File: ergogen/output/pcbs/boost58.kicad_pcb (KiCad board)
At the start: 2 copper layers, 153.6 x 133.5 mm, 110 parts, among them SW1 %R, SW10 %R, SW11 %R, SW12 %R, SW13 %R, SW14 %R, SW15 %R, SW16 %R, SW17 %R, SW18 %R, SW19 %R, SW2 %R, SW20 %R, SW21 %R, SW22 %R, SW23 %R, SW24 %R, SW25 %R, SW26 %R, SW27 %R, SW28 %R, SW29 %R, SW3 %R, SW4 %R, SW5 %R, SW6 %R, SW7 %R, SW8 %R, SW9 %R

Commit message: re-generated PCB
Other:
- board size 153.6 x 133.5 mm -> 147.8 x 127.7 mm

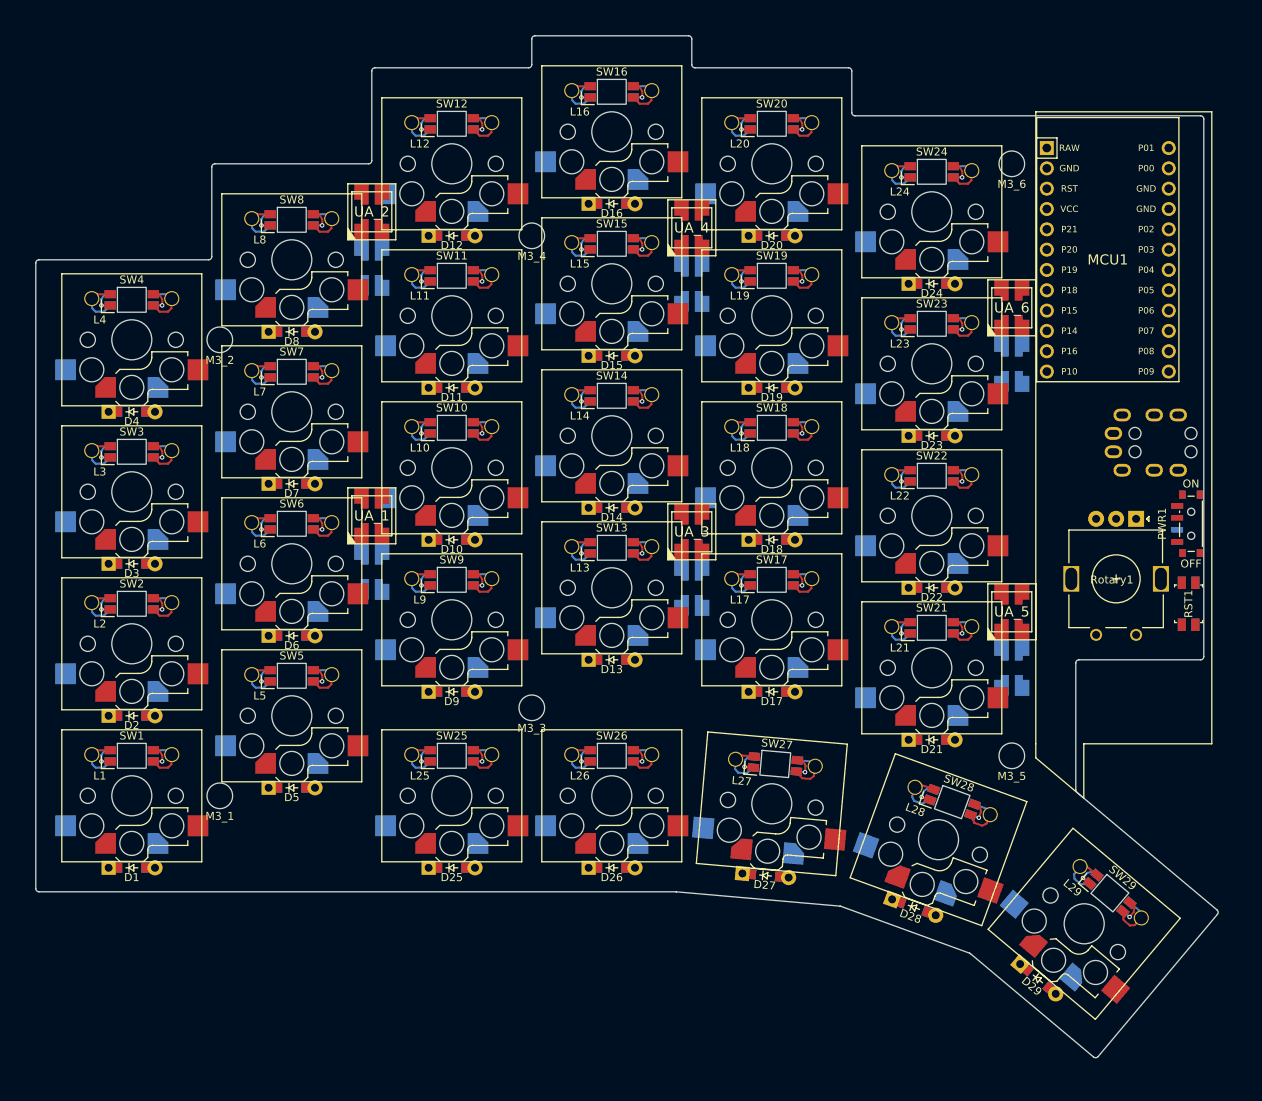
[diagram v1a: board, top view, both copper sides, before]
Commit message: re-generated PCB, and re-ran FreeRouting
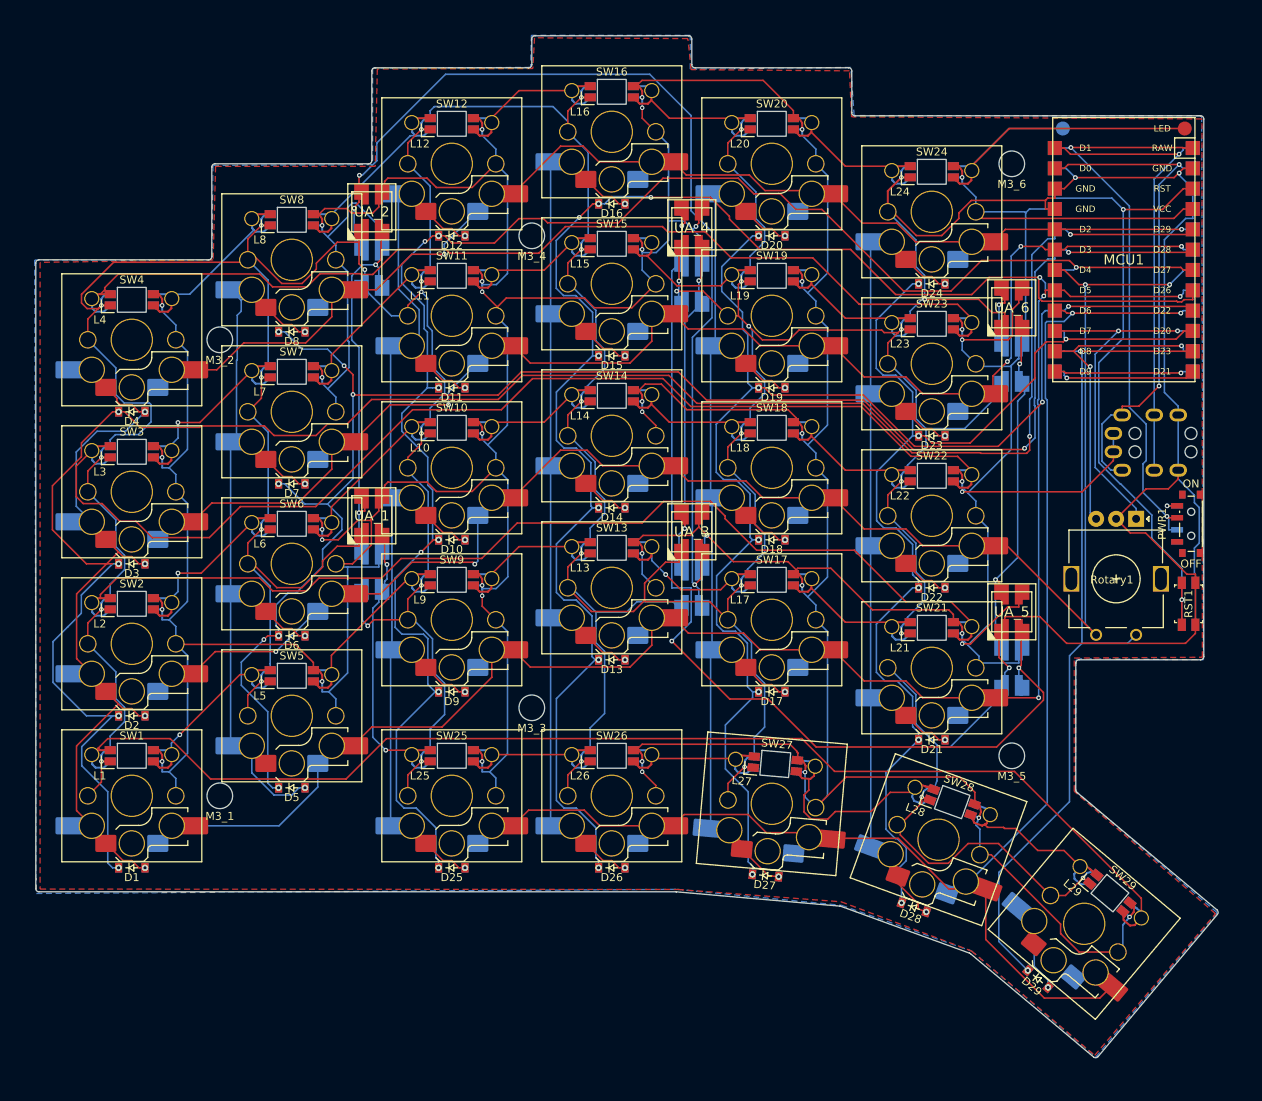
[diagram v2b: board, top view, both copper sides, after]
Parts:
- D1, D10, D11, D12, D13, D14, D15, D16, D17, D18, D19, D2, D20, D21, D22, D23, D24, D25, D26, D27, D28, D29, D3, D4, D5, D6, D7, D8, D9, L1, L10, L11, L12, L13, L14, L15, L16, L17, L18, L19, L2, L20, L21, L22, L23, L24, L25, L26, L27, L28, L29, L3, L4, L5, L6, L7, L8, L9, SW1, SW10, SW11, SW12, SW13, SW14, SW15, SW16, SW17, SW18, SW19, SW2, SW20, SW21, SW22, SW23, SW24, SW25, SW26, SW27, SW28, SW29, SW3, SW4, SW5, SW6, SW7, SW8, SW9: value %R -> ${REFERENCE}
- MCU1: footprint ProMicro -> SparkFunProMicroQwiic
- moved MCU1 2.00 mm to (164.0, 53.0)
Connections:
- net DP14 renamed DD20
- net DP15 renamed DD22
- net DP16 renamed DD23
- net DP18 renamed DD26
- net DP19 renamed DD27
- net DP20 renamed DD28
- net DP21 renamed DD29
- net P1001 renamed LED01
- net P10u01 renamed LEDu01
- net P10u02 renamed LEDu02
- net P10u03 renamed LEDu03
- net P10u04 renamed LEDu04
- net P10u05 renamed LEDu05
- net P10u06 renamed LEDu06
- D1 pad 1: P21 -> D29
- D10 pad 1: P19 -> D27
- D11 pad 1: P19 -> D27
- D12 pad 1: P19 -> D27
- D13 pad 1: P18 -> D26
- D14 pad 1: P18 -> D26
- D15 pad 1: P18 -> D26
- D16 pad 1: P18 -> D26
- D17 pad 1: P15 -> D22
- D18 pad 1: P15 -> D22
- D19 pad 1: P15 -> D22
- D2 pad 1: P21 -> D29
- D20 pad 1: P15 -> D22
- D21 pad 1: P14 -> D20
- D22 pad 1: P14 -> D20
- D23 pad 1: P14 -> D20
- D24 pad 1: P14 -> D20
- D25 pad 1: P19 -> D27
- D26 pad 1: P18 -> D26
- D27 pad 1: P15 -> D22
- D28 pad 1: P14 -> D20
- D29 pad 1: P16 -> D23
- D3 pad 1: P21 -> D29
- D4 pad 1: P21 -> D29
- D5 pad 1: P20 -> D28
- D6 pad 1: P20 -> D28
- D7 pad 1: P20 -> D28
- D8 pad 1: P20 -> D28
- D9 pad 1: P19 -> D27
- L1 pad 2: P1011 -> LED11
- L1 pad 4: P1010 -> LED10
- L10 pad 2: P1023 -> LED23
- L10 pad 4: P1022 -> LED22
- L11 pad 2: P1033 -> LED33
- L11 pad 4: P1032 -> LED32
- L12 pad 2: P1043 -> LED43
- L12 pad 4: P1042 -> LED42
- L13 pad 2: P1014 -> LED14
- L13 pad 4: P1013 -> LED13
- L14 pad 2: P1024 -> LED24
- L14 pad 4: P1023 -> LED23
- L15 pad 2: P1034 -> LED34
- L15 pad 4: P1033 -> LED33
- L16 pad 2: P1044 -> LED44
- L16 pad 4: P1043 -> LED43
- L17 pad 2: P1015 -> LED15
- L17 pad 4: P1014 -> LED14
- L18 pad 2: P1025 -> LED25
- L18 pad 4: P1024 -> LED24
- L19 pad 2: P1035 -> LED35
- L19 pad 4: P1034 -> LED34
- L2 pad 2: P1021 -> LED21
- L2 pad 4: P1020 -> LED20
- L20 pad 2: P1045 -> LED45
- L20 pad 4: P1044 -> LED44
- L21 pad 2: P1020 -> LED20
- L21 pad 4: P1015 -> LED15
- L22 pad 2: P1030 -> LED30
- L22 pad 4: P1025 -> LED25
- L23 pad 2: P1040 -> LED40
- L23 pad 4: P1035 -> LED35
- L24 pad 2: P10 -> LED
- L24 pad 4: P1045 -> LED45
- L25 pad 2: P1002 -> LED02
- L26 pad 2: P1003 -> LED03
- L26 pad 4: P1002 -> LED02
- L27 pad 2: P1004 -> LED04
- L27 pad 4: P1003 -> LED03
- L28 pad 2: P1005 -> LED05
- L28 pad 4: P1004 -> LED04
- L29 pad 2: P1010 -> LED10
- L29 pad 4: P1005 -> LED05
- L3 pad 2: P1031 -> LED31
- L3 pad 4: P1030 -> LED30
- L4 pad 2: P1041 -> LED41
- L4 pad 4: P1040 -> LED40
- L5 pad 2: P1012 -> LED12
- L5 pad 4: P1011 -> LED11
- L6 pad 2: P1022 -> LED22
- L6 pad 4: P1021 -> LED21
- L7 pad 2: P1032 -> LED32
- L7 pad 4: P1031 -> LED31
- L8 pad 2: P1042 -> LED42
- L8 pad 4: P1041 -> LED41
- L9 pad 2: P1013 -> LED13
- L9 pad 4: P1012 -> LED12
- MCU1 pad 1: RAW -> D1
- MCU1 pad 2: GND -> D2
- MCU1 pad 20: P5 -> D20
- MCU1 pad 21: P6 -> D21
- MCU1 pad 22: P7 -> D22
- MCU1 pad 23: P8 -> D23
- MCU1 pad 3: RST -> D3
- MCU1 pad 4: VCC -> D4
- MCU1 pad 5: P21 -> D5
- MCU1 pad 6: P20 -> D6
- MCU1 pad 7: P19 -> D7
- MCU1 pad 8: P18 -> D8
- MCU1 pad 9: P15 -> D9
- Rotary1 pad 1: P16 -> D23
- Rotary1 pad 2: P4 -> D4
- Rotary1 pad A: P7 -> D7
- Rotary1 pad B: P8 -> D8
- SW1 pad : P1011 -> GND
- SW1 pad 1: P5 -> D5
- SW10 pad : P1023 -> GND
- SW10 pad 1: P4 -> D4
- SW11 pad : P1033 -> GND
- SW11 pad 1: P3 -> D3
- SW12 pad : P1043 -> GND
- SW12 pad 1: P2 -> D2
- SW13 pad : P1014 -> GND
- SW13 pad 1: P5 -> D5
- SW14 pad : P1024 -> GND
- SW14 pad 1: P4 -> D4
- SW15 pad : P1034 -> GND
- SW15 pad 1: P3 -> D3
- SW16 pad : P1044 -> GND
- SW16 pad 1: P2 -> D2
- SW17 pad : P1015 -> GND
- SW17 pad 1: P5 -> D5
- SW18 pad : P1025 -> GND
- SW18 pad 1: P4 -> D4
- SW19 pad : P1035 -> GND
- SW19 pad 1: P3 -> D3
- SW2 pad : P1021 -> GND
- SW2 pad 1: P4 -> D4
- SW20 pad : P1045 -> GND
- SW20 pad 1: P2 -> D2
- SW21 pad : P1020 -> GND
- SW21 pad 1: P5 -> D5
- SW22 pad : P1030 -> GND
- SW22 pad 1: P4 -> D4
- SW23 pad : P1040 -> GND
- SW23 pad 1: P3 -> D3
- SW24 pad : P10 -> GND
- SW24 pad 1: P2 -> D2
- SW25 pad : P1002 -> GND
- SW25 pad 1: P6 -> D6
- SW26 pad : P1003 -> GND
- SW26 pad 1: P6 -> D6
- SW27 pad : P1004 -> GND
- SW27 pad 1: P6 -> D6
- SW28 pad : P1005 -> GND
- SW28 pad 1: P6 -> D6
- SW29 pad : P1010 -> GND
- SW29 pad 1: P6 -> D6
- SW3 pad : P1031 -> GND
- SW3 pad 1: P3 -> D3
- SW4 pad : P1041 -> GND
- SW4 pad 1: P2 -> D2
- SW5 pad : P1012 -> GND
- SW5 pad 1: P5 -> D5
- SW6 pad : P1022 -> GND
- SW6 pad 1: P4 -> D4
- SW7 pad : P1032 -> GND
- SW7 pad 1: P3 -> D3
- SW8 pad : P1042 -> GND
- SW8 pad 1: P2 -> D2
- SW9 pad : P1013 -> GND
- SW9 pad 1: P5 -> D5
- TRRS1 pad 2: P0 -> D0
- TRRS1 pad 3: P1 -> D1
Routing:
- net GND: track 96.3 -> 1040.1 mm, vias 29 -> 39
- net VCC: track 96.3 -> 964.8 mm, vias 29 -> 40
- net D29: track 0.00 -> 249.3 mm, vias 0 -> 6
- net D5: track 0.00 -> 219.0 mm, vias 0 -> 3
- net D4: track 0.00 -> 215.6 mm, vias 0 -> 4
- net D28: track 0.00 -> 215.4 mm, vias 0 -> 9
- net D27: track 0.00 -> 208.9 mm, vias 0 -> 8
- net D6: track 0.00 -> 204.4 mm, vias 0 -> 2
- net D26: track 0.00 -> 192.9 mm, vias 0 -> 8
- net D3: track 0.00 -> 181.2 mm, vias 0 -> 4
- net D22: track 0.00 -> 169.4 mm, vias 0 -> 7
- net LED10: track 0.00 -> 162.7 mm
- net D2: track 0.00 -> 162.4 mm, vias 0 -> 2
- net LED30: track 0.00 -> 148.6 mm
- net D20: track 0.00 -> 142.2 mm, vias 0 -> 6
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- added copper zone on F.Cu, net GND
- added copper zone on B.Cu, net VCC

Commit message: re-generated pcb's and outlines
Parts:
- removed UA_1, UA_2, UA_3, UA_4, UA_5, UA_6, UB_1, UB_2, UB_3, UB_4, UB_5, UB_6: , WS2812B
- added U_1: , WS2812B, F.Cu at (68.0, 89.0)
- added U_2: , WS2812B, F.Cu at (68.0, 51.0)
- added U_3: , WS2812B, F.Cu at (107.0, 89.0)
- added U_4: , WS2812B, F.Cu at (107.0, 51.0)
- added U_5: , WS2812B, F.Cu at (146.0, 97.0)
- added U_6: , WS2812B, F.Cu at (146.0, 59.0)
- D1, D10, D11, D12, D13, D14, D15, D16, D17, D18, D19, D2, D20, D21, D22, D23, D24, D25, D26, D27, D28, D29, D3, D4, D5, D6, D7, D8, D9, L1, L10, L11, L12, L13, L14, L15, L16, L17, L18, L19, L2, L20, L21, L22, L23, L24, L25, L26, L27, L28, L29, L3, L4, L5, L6, L7, L8, L9, SW1, SW10, SW11, SW12, SW13, SW14, SW15, SW16, SW17, SW18, SW19, SW2, SW20, SW21, SW22, SW23, SW24, SW25, SW26, SW27, SW28, SW29, SW3, SW4, SW5, SW6, SW7, SW8, SW9: value ${REFERENCE} -> %R
- MCU1: footprint SparkFunProMicroQwiic -> ProMicro
- moved D21 17.0 mm to (127.0, 102.0), turned to -90 degrees
- moved D22 17.0 mm to (127.0, 83.0), turned to -90 degrees
- moved D23 17.0 mm to (127.0, 64.0), turned to -90 degrees
- moved D24 17.0 mm to (127.0, 45.0), turned to -90 degrees
- moved D17 16.3 mm to (108.0, 96.0), turned to -90 degrees
- moved D18 16.3 mm to (108.0, 77.0), turned to -90 degrees
- moved D19 16.3 mm to (108.0, 58.0), turned to -90 degrees
- moved D20 16.3 mm to (108.0, 39.0), turned to -90 degrees
- moved D13 15.6 mm to (89.0, 92.0), turned to -90 degrees
- moved D14 15.6 mm to (89.0, 73.0), turned to -90 degrees
- moved D15 15.6 mm to (89.0, 54.0), turned to -90 degrees
- moved D16 15.6 mm to (89.0, 35.0), turned to -90 degrees
- moved D27 14.9 mm to (109.0, 119.1), turned to -95 degrees
- moved D10 14.9 mm to (70.0, 77.0), turned to -90 degrees
- moved D11 14.9 mm to (70.0, 58.0), turned to -90 degrees
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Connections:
- D1 pad 1: D29 -> P21
- D1 pad 2: DD29 -> DP21
- D10 pad 1: D27 -> P19
- D10 pad 2: DD27 -> DP19
- D11 pad 1: D27 -> P19
- D11 pad 2: DD27 -> DP19
- D12 pad 1: D27 -> P19
- D12 pad 2: DD27 -> DP19
- D13 pad 1: D26 -> P18
- D13 pad 2: DD26 -> DP18
- D14 pad 1: D26 -> P18
- D14 pad 2: DD26 -> DP18
- D15 pad 1: D26 -> P18
- D15 pad 2: DD26 -> DP18
- D16 pad 1: D26 -> P18
- D16 pad 2: DD26 -> DP18
- D17 pad 1: D22 -> P15
- D17 pad 2: DD22 -> DP15
- D18 pad 1: D22 -> P15
- D18 pad 2: DD22 -> DP15
- D19 pad 1: D22 -> P15
- D19 pad 2: DD22 -> DP15
- D2 pad 1: D29 -> P21
- D2 pad 2: DD29 -> DP21
- D20 pad 1: D22 -> P15
- D20 pad 2: DD22 -> DP15
- D21 pad 1: D20 -> P14
- D21 pad 2: DD20 -> DP14
- D22 pad 1: D20 -> P14
- D22 pad 2: DD20 -> DP14
- D23 pad 1: D20 -> P14
- D23 pad 2: DD20 -> DP14
- D24 pad 1: D20 -> P14
- D24 pad 2: DD20 -> DP14
- D25 pad 1: D27 -> P21
- D25 pad 2: DD27 -> DP21
- D26 pad 1: D26 -> P20
- D26 pad 2: DD26 -> DP20
- D27 pad 1: D22 -> P19
- D27 pad 2: DD22 -> DP19
- D28 pad 1: D20 -> P18
- D28 pad 2: DD20 -> DP18
- D29 pad 1: D23 -> P15
- D29 pad 2: DD23 -> DP15
- D3 pad 1: D29 -> P21
- D3 pad 2: DD29 -> DP21
- D4 pad 1: D29 -> P21
- D4 pad 2: DD29 -> DP21
- D5 pad 1: D28 -> P20
- D5 pad 2: DD28 -> DP20
- D6 pad 1: D28 -> P20
- D6 pad 2: DD28 -> DP20
- D7 pad 1: D28 -> P20
- D7 pad 2: DD28 -> DP20
- D8 pad 1: D28 -> P20
- D8 pad 2: DD28 -> DP20
- D9 pad 1: D27 -> P19
- D9 pad 2: DD27 -> DP19
- MCU1 pad 1: D1 -> RAW
- MCU1 pad 2: D2 -> GND
- MCU1 pad 20: D20 -> P2
- MCU1 pad 21: D21 -> GND
- MCU1 pad 22: D22 -> GND
- MCU1 pad 23: D23 -> P0
- MCU1 pad 3: D3 -> RST
- MCU1 pad 4: D4 -> VCC
- MCU1 pad 5: D5 -> P21
- MCU1 pad 6: D6 -> P20
- MCU1 pad 7: D7 -> P19
- MCU1 pad 8: D8 -> P18
- MCU1 pad 9: D9 -> P15
- Rotary1 pad 1: D23 -> P14
- Rotary1 pad 2: D4 -> P6
- Rotary1 pad A: D7 -> P7
- Rotary1 pad B: D8 -> P8
- SW1 pad : GND -> LED11
- SW1 pad 1: D5 -> P5
- SW1 pad 2: DD29 -> DP21
- SW10 pad : GND -> LED23
- SW10 pad 1: D4 -> P4
- SW10 pad 2: DD27 -> DP19
- SW11 pad : GND -> LED33
- SW11 pad 1: D3 -> P3
- SW11 pad 2: DD27 -> DP19
- SW12 pad : GND -> LED43
- SW12 pad 1: D2 -> P2
- SW12 pad 2: DD27 -> DP19
- SW13 pad : GND -> LED14
- SW13 pad 1: D5 -> P5
- SW13 pad 2: DD26 -> DP18
- SW14 pad : GND -> LED24
- SW14 pad 1: D4 -> P4
- SW14 pad 2: DD26 -> DP18
- SW15 pad : GND -> LED34
- SW15 pad 1: D3 -> P3
- SW15 pad 2: DD26 -> DP18
- SW16 pad : GND -> LED44
- SW16 pad 1: D2 -> P2
- SW16 pad 2: DD26 -> DP18
- SW17 pad : GND -> LED15
- SW17 pad 1: D5 -> P5
- SW17 pad 2: DD22 -> DP15
- SW18 pad : GND -> LED25
- SW18 pad 1: D4 -> P4
- SW18 pad 2: DD22 -> DP15
- SW19 pad : GND -> LED35
- SW19 pad 1: D3 -> P3
- SW19 pad 2: DD22 -> DP15
- SW2 pad : GND -> LED21
- SW2 pad 1: D4 -> P4
- SW2 pad 2: DD29 -> DP21
- SW20 pad : GND -> LED45
- SW20 pad 1: D2 -> P2
- SW20 pad 2: DD22 -> DP15
- SW21 pad : GND -> LED20
- SW21 pad 1: D5 -> P5
- SW21 pad 2: DD20 -> DP14
- SW22 pad : GND -> LED30
- SW22 pad 1: D4 -> P4
- SW22 pad 2: DD20 -> DP14
- SW23 pad : GND -> LED40
- SW23 pad 1: D3 -> P3
- SW23 pad 2: DD20 -> DP14
- SW24 pad : GND -> LED
- SW24 pad 1: D2 -> P2
- SW24 pad 2: DD20 -> DP14
- SW25 pad : GND -> LED02
- SW25 pad 1: D6 -> P6
- SW25 pad 2: DD27 -> DP21
- SW26 pad : GND -> LED03
- SW26 pad 1: D6 -> P6
- SW26 pad 2: DD26 -> DP20
- SW27 pad : GND -> LED04
- SW27 pad 1: D6 -> P6
- SW27 pad 2: DD22 -> DP19
- SW28 pad : GND -> LED05
- SW28 pad 1: D6 -> P6
- SW28 pad 2: DD20 -> DP18
- SW29 pad : GND -> LED10
- SW29 pad 1: D6 -> P6
- SW29 pad 2: DD23 -> DP15
- SW3 pad : GND -> LED31
- SW3 pad 1: D3 -> P3
- SW3 pad 2: DD29 -> DP21
- SW4 pad : GND -> LED41
- SW4 pad 1: D2 -> P2
- SW4 pad 2: DD29 -> DP21
- SW5 pad : GND -> LED12
- SW5 pad 1: D5 -> P5
- SW5 pad 2: DD28 -> DP20
- SW6 pad : GND -> LED22
- SW6 pad 1: D4 -> P4
- SW6 pad 2: DD28 -> DP20
- SW7 pad : GND -> LED32
- SW7 pad 1: D3 -> P3
- SW7 pad 2: DD28 -> DP20
- SW8 pad : GND -> LED42
- SW8 pad 1: D2 -> P2
- SW8 pad 2: DD28 -> DP20
- SW9 pad : GND -> LED13
- SW9 pad 1: D5 -> P5
- SW9 pad 2: DD27 -> DP19
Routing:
- net GND: track 1040.1 -> 96.3 mm, vias 39 -> 29
- net VCC: track 964.8 -> 96.3 mm, vias 40 -> 29
- net D29: track 249.3 -> 0.00 mm, vias 6 -> 0
- net D5: track 219.0 -> 0.00 mm, vias 3 -> 0
- net D4: track 215.6 -> 0.00 mm, vias 4 -> 0
- net D28: track 215.4 -> 0.00 mm, vias 9 -> 0
- net D27: track 208.9 -> 0.00 mm, vias 8 -> 0
- net D6: track 204.4 -> 0.00 mm, vias 2 -> 0
- net D26: track 192.9 -> 0.00 mm, vias 8 -> 0
- net D3: track 181.2 -> 0.00 mm, vias 4 -> 0
- net D22: track 169.4 -> 0.00 mm, vias 7 -> 0
- net D2: track 162.4 -> 0.00 mm, vias 2 -> 0
- net LED10: track 162.7 -> 13.5 mm
- net D20: track 142.2 -> 0.00 mm, vias 6 -> 0
- net DD26: track 141.7 -> 0.00 mm, vias 5 -> 0
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- removed copper zone on F.Cu, net GND
- removed copper zone on B.Cu, net VCC
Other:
- board size 147.8 x 127.7 mm -> 144.3 x 128.5 mm
